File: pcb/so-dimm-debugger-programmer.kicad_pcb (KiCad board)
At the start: 2 copper layers, 105.3 x 76.5 mm, 35 parts, among them J1 1612618-4, J2 Conn_01x06_Male, J3 Conn_01x06_Male, J4 Conn_01x04_Male, J5 Conn_01x04_Male, J6 USB4105-GF-A, J7 USB4105-GF-A, J8 Conn_02x16_Odd_Even, Q1 UMH3N, U1 AP2112K-3.3, U2 USBLC6-2P6, U3 USBLC6-2P6, U4 CP2102N-Axx-xQFN28

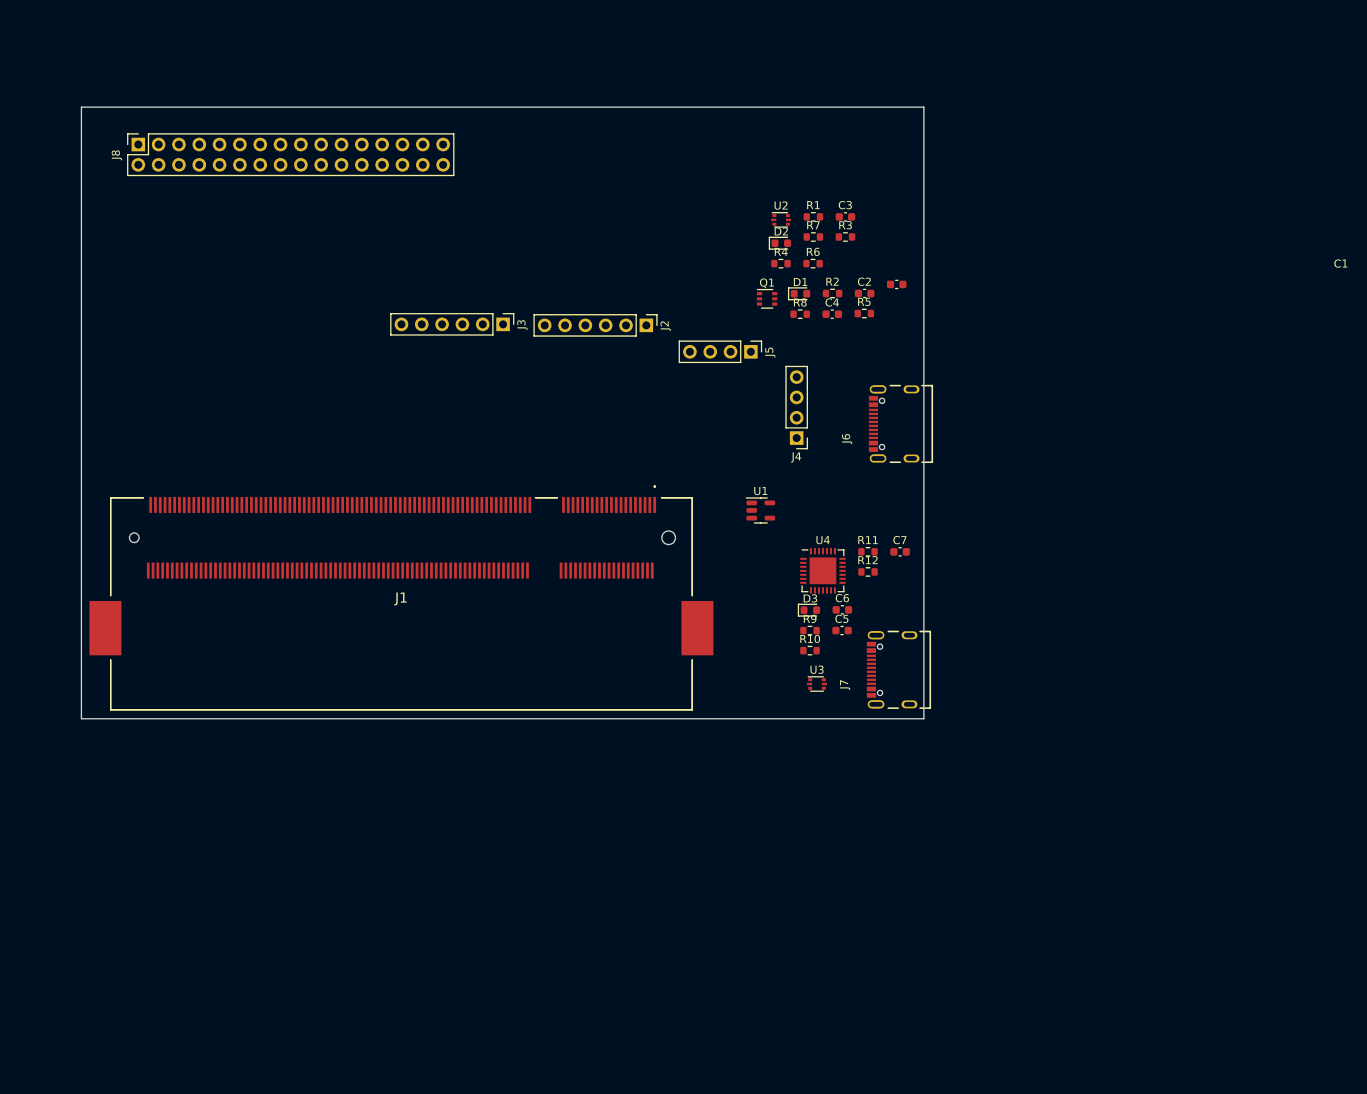
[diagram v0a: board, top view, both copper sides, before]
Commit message: Added first version of the pcb layout
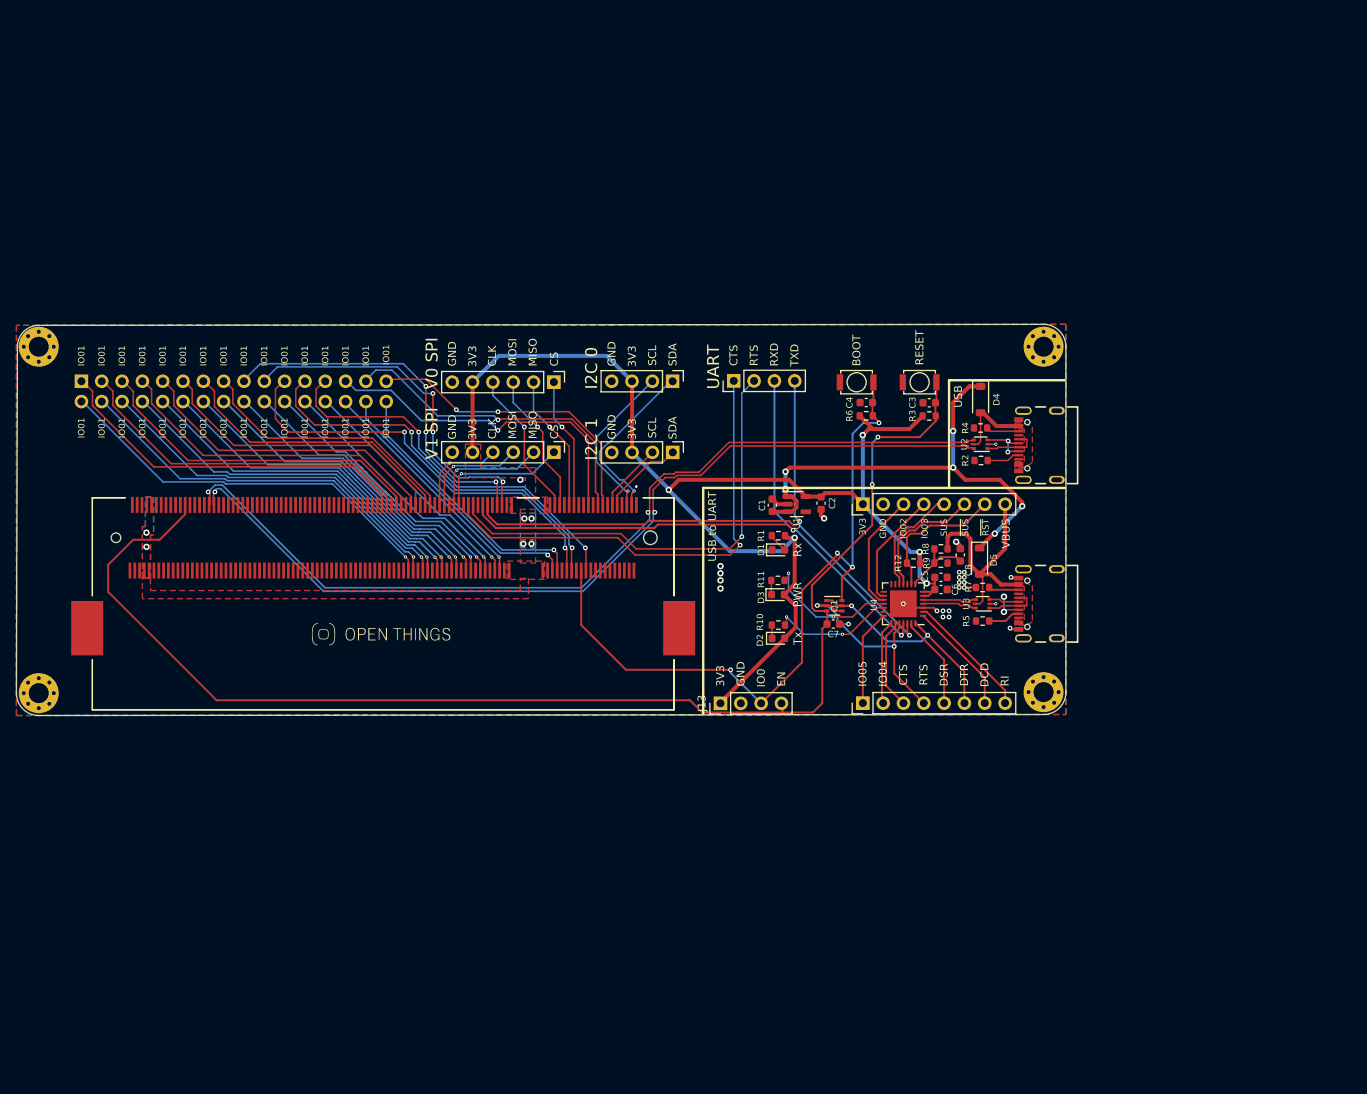
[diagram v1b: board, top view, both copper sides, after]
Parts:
- added C8: 1uF, Capacitor_SMD:C_0603_1608Metric, F.Cu at (194.9, 104.9)
- added D4: 1N5819HW-7-F, Diode_SMD:D_SOD-123, F.Cu at (197.5, 85.5)
- added D5: 1N5819HW-7-F, Diode_SMD:D_SOD-123, F.Cu at (197.4, 105.7)
- added G1: LOGO, LOGO, F.Cu at (122.8, 114.8)
- added H1: MH/DNP, MountingHole:MountingHole_2.5mm_Pad_Via, F.Cu at (205.4, 122.0)
- added H2: MH/DNP, MountingHole:MountingHole_2.5mm_Pad_Via, F.Cu at (79.8, 122.2)
- added H3: MH/DNP, MountingHole:MountingHole_2.5mm_Pad_Via, F.Cu at (205.4, 78.9)
- added H4: MH/DNP, MountingHole:MountingHole_2.5mm_Pad_Via, F.Cu at (79.8, 78.9)
- added J10: Conn_01x08_Male, Connector_PinHeader_2.54mm:PinHeader_1x08_P2.54mm_Vertical, F.Cu at (182.8, 98.6)
- added J11: Conn_01x08_Male, Connector_PinHeader_2.54mm:PinHeader_1x08_P2.54mm_Vertical, F.Cu at (182.8, 123.4)
- added J12: UART, Connector_PinHeader_2.54mm:PinHeader_1x04_P2.54mm_Vertical, F.Cu at (166.6, 83.1)
- added J13: Conn_01x04_Pin, Connector_PinHeader_2.54mm:PinHeader_1x04_P2.54mm_Vertical, F.Cu at (165.0, 123.4)
- added SW1: SW_Push, SKRKAEE020:SKRKAEE020, F.Cu at (189.9, 83.3)
- added SW2: SW_Push, SKRKAEE020:SKRKAEE020, F.Cu at (182.0, 83.3)
- C3, C4: value 4.7nF -> 0.1uF
- J2: value Conn_01x06_Male -> V0_SPI
- J3: value Conn_01x06_Male -> V1_SPI
- J4: value Conn_01x04_Male -> I2C_0
- J5: value Conn_01x04_Male -> I2C_1
- J8: footprint Connector_PinSocket_2.54mm:PinSocket_2x16_P2.54mm_Vertical -> Connector_PinHeader_2.54mm:PinHeader_2x16_P2.54mm_Vertical; moved to B.Cu
- R3, R6: value 1M -> 10k
- moved D2 49.4 mm to (172.2, 115.3)
- moved R7 48.7 mm to (197.7, 109.0)
- moved R5 41.2 mm to (197.7, 113.2)
- moved R1 40.1 mm to (172.2, 102.5)
- moved Q1 39.3 mm to (179.2, 111.3)
- moved U2 37.5 mm to (197.5, 91.1), turned to 180 degrees
- moved R8 34.2 mm to (192.5, 104.1)
- moved R4 32.3 mm to (197.5, 89.0)
- moved D1 32.1 mm to (172.2, 104.3)
- moved C1 31.7 mm to (171.4, 98.7), turned to 90 degrees
- moved J8 30.4 mm to (85.1, 83.2), turned to -90 degrees
- moved R2 27.9 mm to (197.5, 93.1)
- moved C2 26.8 mm to (177.5, 98.4), turned to -90 degrees
- moved C3 25.5 mm to (191.1, 85.9), turned to 180 degrees
- moved R3 24.7 mm to (191.1, 87.5), turned to 180 degrees
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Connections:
- net Net-(R12-Pad1) renamed /usb-to-uart/~{RST}
- C1 pad 1: VBUS -> +5V
- C3 pad 1: Net-(C3-Pad1) -> /EN
- C4 pad 1: Net-(C4-Pad1) -> /IO0
- J1 pad 57: unconnected-(J1-Pad57) -> /GPIO15/RTS
- J1 pad 59: unconnected-(J1-Pad59) -> /GPIO16/CTS
- J6 pad A4_B9: VBUS -> /usb-ports/VBUSB
- J6 pad B4_A9: VBUS -> /usb-ports/VBUSB
- J6 pad S1: Net-(C3-Pad1) -> unconnected-(J6-SHELL_GND-PadS1)
- J7 pad S1: Net-(C4-Pad1) -> unconnected-(J7-SHELL_GND-PadS1)
- J8 pad 1: /E1_IO0_00 -> /E2_IO0_01
- J8 pad 10: /E2_IO0_04 -> /E2_IO1_04
- J8 pad 11: /E1_IO0_05 -> /E1_IO1_00
- J8 pad 12: /E2_IO0_05 -> /E2_IO1_05
- J8 pad 13: /E1_IO0_06 -> /E1_IO1_04
- J8 pad 14: /E2_IO0_06 -> /E2_IO1_06
- J8 pad 15: /E1_IO0_07 -> /E1_IO1_05
- J8 pad 16: /E2_IO0_07 -> /E2_IO1_07
- J8 pad 17: /E1_IO1_00 -> /E1_IO1_06
- J8 pad 18: /E2_IO1_00 -> /E2_IO0_07
- J8 pad 19: /E1_IO1_01 -> /E1_IO1_07
- J8 pad 2: /E2_IO0_00 -> /E2_IO1_00
- J8 pad 20: /E2_IO1_01 -> /E2_IO0_06
- J8 pad 21: /E1_IO1_02 -> /E1_IO0_05
- J8 pad 22: /E2_IO1_02 -> /E2_IO0_05
- J8 pad 23: /E1_IO1_03 -> /E1_IO0_04
- J8 pad 24: /E2_IO1_03 -> /E2_IO0_04
- J8 pad 25: /E1_IO1_04 -> /E1_IO0_03
- J8 pad 26: /E2_IO1_04 -> /E2_IO0_03
- J8 pad 27: /E1_IO1_05 -> /E1_IO0_02
- J8 pad 28: /E2_IO1_05 -> /E2_IO0_02
- J8 pad 29: /E1_IO1_06 -> /E1_IO0_01
- J8 pad 3: /E1_IO0_01 -> /E2_IO0_00
- J8 pad 30: /E2_IO1_06 -> /E1_IO0_07
- J8 pad 31: /E1_IO1_07 -> /E1_IO0_00
- J8 pad 32: /E2_IO1_07 -> /E1_IO0_06
- J8 pad 4: /E2_IO0_01 -> /E2_IO1_01
- J8 pad 5: /E1_IO0_02 -> /E1_IO1_03
- J8 pad 6: /E2_IO0_02 -> /E2_IO1_02
- J8 pad 7: /E1_IO0_03 -> /E1_IO1_02
- J8 pad 8: /E2_IO0_03 -> /E2_IO1_03
- J8 pad 9: /E1_IO0_04 -> /E1_IO1_01
- R3 pad 1: GND -> /EN
- R3 pad 2: Net-(C3-Pad1) -> +3V3
- R6 pad 1: GND -> /IO0
- R6 pad 2: Net-(C4-Pad1) -> +3V3
- U1 pad 1: VBUS -> +5V
- U1 pad 3: VBUS -> +5V
- U2 pad 5: VBUS -> /usb-ports/VBUSB
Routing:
- net /EN: track 0.00 -> 165.5 mm, vias 0 -> 2
- net +3V3: track 0.00 -> 160.6 mm, vias 0 -> 11
- net /ESP_USB_D-: track 0.00 -> 113.6 mm, vias 0 -> 2
- net /ESP_USB_D+: track 0.00 -> 112.5 mm, vias 0 -> 2
- net /IO0: track 0.00 -> 89.7 mm, vias 0 -> 4
- net /RXD: track 0.00 -> 81.4 mm, vias 0 -> 2
- net /TXD: track 0.00 -> 80.7 mm, vias 0 -> 2
- net +5V: track 0.00 -> 60.6 mm, vias 0 -> 6
- net /GPIO16/CTS: track 0.00 -> 58.7 mm, vias 0 -> 1
- net /GPIO15/RTS: track 0.00 -> 57.3 mm, vias 0 -> 1
- net /E1_IO0_05: track 0.00 -> 52.8 mm, vias 0 -> 2
- net /E2_IO1_00: track 0.00 -> 50.5 mm, vias 0 -> 1
- net /E1_IO0_04: track 0.00 -> 50.1 mm, vias 0 -> 2
- net /E2_IO1_01: track 0.00 -> 48.8 mm, vias 0 -> 1
- net /E1_IO0_03: track 0.00 -> 48.8 mm, vias 0 -> 2
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- added copper zone on B.Cu, net +3V3
- added copper zone on F.Cu, net +3V3
- added copper zone on F.Cu, net /usb-ports/VBUSB
- added copper zone on B.Cu, net GND
- added copper zone on F.Cu, net GND
- added copper zone on F.Cu, net VBUS
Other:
- board size 105.3 x 76.5 mm -> 131.2 x 48.9 mm
- board text added: "3V3"
- board text added: "BOOT"
- board text added: "CLK"
- board text added: "CS"
- board text added: "CTS"
- board text added: "DCD"
- board text added: "DSR"
- board text added: "DTR"
- board text added: "EN"
- board text added: "GND"
- board text added: "I2C 0"
- board text added: "I2C 1"
- board text added: "IO0"
- board text added: "IO01"
- board text added: "IO02"
- board text added: "IO03"
- board text added: "IO04"
- board text added: "IO05"
- board text added: "MISO"
- board text added: "MOSI"
- board text added: "PWR"
- board text added: "RESET"
- board text added: "RI"
- board text added: "RTS"
- board text added: "RXD"
- board text added: "Rx"
- board text added: "SCL"
- board text added: "SDA"
- board text added: "SUS"
- board text added: "TXD"
- board text added: "Tx"
- board text added: "UART"
- board text added: "USB"
- board text added: "USB to UART"
- board text added: "V0 SPI"
- board text added: "V1 SPI"
- board text added: "VBUS"
- board text added: "~{RST}"
- board text added: "~{SUS}"

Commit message: Finished up board layout
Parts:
- moved H1 117.2 mm to (96.7, 166.0), turned to -90 degrees
- moved J7 114.3 mm to (107.8, 167.6), turned to 0 degrees
- moved J6 110.3 mm to (127.6, 167.6), turned to 0 degrees
- moved H3 109.0 mm to (139.9, 166.0), turned to -90 degrees
- moved R5 102.6 mm to (105.6, 158.4), turned to -90 degrees
- moved U3 101.7 mm to (107.8, 158.4), turned to 90 degrees
- moved R7 100.9 mm to (109.8, 158.4), turned to -90 degrees
- moved D5 99.2 mm to (113.1, 158.0), turned to 180 degrees
- moved R2 97.0 mm to (125.7, 158.2), turned to -90 degrees
- moved D4 96.9 mm to (133.3, 158.1), turned to 180 degrees
- moved U2 96.8 mm to (127.7, 158.1), turned to 90 degrees
- moved R4 96.8 mm to (129.7, 158.1), turned to -90 degrees
- moved C8 95.6 mm to (113.9, 155.6), turned to 0 degrees
- moved C6 93.9 mm to (109.5, 153.1), turned to -90 degrees
- moved C5 93.3 mm to (111.1, 153.1), turned to -90 degrees
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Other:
- board size 131.2 x 48.9 mm -> 48.9 x 131.2 mm
- board text added: "IO06"
- board text added: "IO07"
- board text added: "IO08"
- board text added: "IO09"
- board text added: "IO10"
- board text added: "IO11"
- board text added: "IO12"
- board text added: "IO13"
- board text added: "IO14"
- board text added: "IO15"
- board text added: "IO16"
- board text added: "IO17"
- board text added: "IO18"
- board text added: "IO19"
- board text added: "IO20"
- board text added: "IO21"
- board text added: "IO22"
- board text added: "IO23"
- board text added: "IO24"
- board text added: "IO25"
- board text added: "IO26"
- board text added: "IO27"
- board text added: "IO28"
- board text added: "IO29"
- board text added: "IO30"
- board text added: "IO31"
- board text added: "IO32"

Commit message: Try to fix all ERC and DRC Issues and Warning + changed violation config
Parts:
- removed J11: Conn_01x08_Male, Connector_PinHeader_2.54mm:PinHeader_1x08_P2.54mm_Vertical
- added J9: Conn_01x04_Pin, Connector_PinHeader_2.54mm:PinHeader_1x04_P2.54mm_Vertical, F.Cu at (135.6, 127.3)
- J10: value Conn_01x08_Male -> Conn_01x08_Pin
- J12: value UART -> Conn_01x06_Pin; footprint Connector_PinHeader_2.54mm:PinHeader_1x04_P2.54mm_Vertical -> Connector_PinHeader_2.54mm:PinHeader_1x06_P2.54mm_Vertical
- J2: value V0_SPI -> Conn_01x06_Pin
- J3: value V1_SPI -> Conn_01x04_Pin; footprint Connector_PinHeader_2.54mm:PinHeader_1x06_P2.54mm_Vertical -> Connector_PinHeader_2.54mm:PinHeader_1x04_P2.54mm_Vertical
- J4: value I2C_0 -> Conn_01x04_Pin
- J5: value I2C_1 -> Conn_01x08_Pin; footprint Connector_PinHeader_2.54mm:PinHeader_1x04_P2.54mm_Vertical -> Connector_PinHeader_2.54mm:PinHeader_1x08_P2.54mm_Vertical
- moved J10 24.9 mm to (95.2, 143.4)
- moved J5 24.6 mm to (120.3, 143.4), turned to 0 degrees
- moved J12 22.5 mm to (135.5, 104.8), turned to 180 degrees
- moved J3 17.3 mm to (135.5, 119.6)
- moved J4 8.94 mm to (126.6, 119.6)
- moved J2 8.84 mm to (126.6, 104.8)
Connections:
- J10 pad 1: +3V3 -> /usb-to-uart/GPIO05
- J10 pad 2: GND -> /usb-to-uart/GPIO04
- J10 pad 3: /usb-to-uart/GPIO02 -> /usb-to-uart/CTS
- J10 pad 4: /usb-to-uart/GPIO03 -> /usb-to-uart/RTS
- J10 pad 5: /usb-to-uart/SUSPEND -> /usb-to-uart/DSR
- J10 pad 6: /usb-to-uart/~{SUSPEND} -> /usb-to-uart/DTR
- J10 pad 7: /usb-to-uart/~{RST} -> /usb-to-uart/DCD
- J10 pad 8: VBUS -> /usb-to-uart/RI
- J12 pad 1: /GPIO16/CTS -> /V0SPI_CS
- J12 pad 2: /GPIO15/RTS -> /V0SPI_MISO
- J12 pad 3: /RXD -> /V0SPI_MOSI
- J12 pad 4: /TXD -> /V0SPI_CLK
- J2 pad 1: /V0SPI_CS -> /V1SPI_CS
- J2 pad 2: /V0SPI_MISO -> /V1SPI_MISO
- J2 pad 3: /V0SPI_MOSI -> /V1SPI_MOSI
- J2 pad 4: /V0SPI_CLK -> /V1SPI_CLK
- J3 pad 1: /V1SPI_CS -> /SDA0
- J3 pad 2: /V1SPI_MISO -> /SCL0
- J3 pad 3: /V1SPI_MOSI -> +3V3
- J3 pad 4: /V1SPI_CLK -> GND
- J4 pad 1: /SDA0 -> /SDA1
- J4 pad 2: /SCL0 -> /SCL1
- J5 pad 1: /SDA1 -> +3V3
- J5 pad 2: /SCL1 -> GND
- J5 pad 3: +3V3 -> /usb-to-uart/GPIO02
- J5 pad 4: GND -> /usb-to-uart/GPIO03
